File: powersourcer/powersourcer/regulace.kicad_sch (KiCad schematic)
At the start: 47 parts, among them Q1 2N2222, Q10 TIP35C, Q2 TIP122, Q3 TIP35C, Q4 TIP35C, Q5 TIP35C, Q6 TIP35C, Q7 TIP35C, Q8 TIP35C, Q9 TIP35C, U1 LM336Z-5.0, U2 TL081

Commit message: První návrh pcb.
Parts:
- C1, C2: footprint (none) -> Capacitor_SMD:C_1206_3216Metric_Pad1.33x1.80mm_HandSolder
- C3, C5: footprint (none) -> HAM_Lib:CP_Radial_D10.0mm_P5.00mm
- C4: footprint (none) -> HAM_Lib:CP_Radial_D8.0mm_P5.00mm
- H1, H2, H3, H4, H5, H6: footprint (none) -> HAM_Lib:PinHeader_1x01_P1.00mm_Vertical
- Q10, Q3, Q4, Q5, Q6, Q7, Q8, Q9: footprint HAM_Lib:TO-247-3_Vertical -> HAM_Lib:TO-247-3_Horizontal_TabUp
- R6: footprint (none) -> HAM_Lib:R_Radial_Power_L13.0mm_W9.0mm_P5.00mm
- RV1: footprint (none) -> HAM_Lib:Potentiometer_Bourns_3296W_Vertical
- U2: footprint (none) -> HAM_Lib:DIP-8_W7.62mm
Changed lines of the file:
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@@
 			)
 		)
-		(property "Footprint" ""
+		(property "Footprint" "HAM_Lib:PinHeader_1x01_P1.00mm_Vertical"
 			(at 20.32 24.13 0)
 			(hide yes)
@@
 			)
 		)
-		(property "Footprint" ""
+		(property "Footprint" "HAM_Lib:R_Radial_Power_L13.0mm_W9.0mm_P5.00mm"
 			(at 96.012 36.83 90)
 			(hide yes)
@@
 			)
 		)
-		(property "Footprint" ""
+		(property "Footprint" "HAM_Lib:DIP-8_W7.62mm"
 			(at 63.5 48.26 0)
 			(hide yes)
@@
 			)
 		)
-		(property "Footprint" ""
+		(property "Footprint" "HAM_Lib:CP_Radial_D10.0mm_P5.00mm"
 			(at 221.9452 35.56 0)
 			(hide yes)
@@
 			)
 		)
-		(property "Footprint" ""
+		(property "Footprint" "HAM_Lib:PinHeader_1x01_P1.00mm_Vertical"
 			(at 269.24 39.37 0)
 			(hide yes)
@@
 			)
 		)
-		(property "Footprint" ""
+		(property "Footprint" "HAM_Lib:PinHeader_1x01_P1.00mm_Vertical"
 			(at 113.03 41.91 0)
 			(hide yes)
@@
 			)
 		)
-		(property "Footprint" "HAM_Lib:TO-247-3_Vertical"
+		(property "Footprint" "HAM_Lib:TO-247-3_Horizontal_TabUp"
 			(at 237.49 60.325 0)
 			(hide yes)
@@
 			)
 		)
-		(property "Footprint" "HAM_Lib:TO-247-3_Vertical"
+		(property "Footprint" "HAM_Lib:TO-247-3_Horizontal_TabUp"
 			(at 219.71 60.325 0)
 			(hide yes)
@@
 			)
 		)
-		(property "Footprint" ""
+		(property "Footprint" "Capacitor_SMD:C_1206_3216Metric_Pad1.33x1.80mm_HandSolder"
 			(at 69.85 34.5948 0)
 			(hide yes)
@@
 			)
 		)
-		(property "Footprint" "HAM_Lib:TO-247-3_Vertical"
+		(property "Footprint" "HAM_Lib:TO-247-3_Horizontal_TabUp"
 			(at 201.93 60.325 0)
 			(hide yes)
@@
 			)
 		)
-		(property "Footprint" "HAM_Lib:TO-247-3_Vertical"
+		(property "Footprint" "HAM_Lib:TO-247-3_Horizontal_TabUp"
 			(at 166.37 60.325 0)
 			(hide yes)
@@
 			)
 		)
-		(property "Footprint" "HAM_Lib:TO-247-3_Vertical"
+		(property "Footprint" "HAM_Lib:TO-247-3_Horizontal_TabUp"
 			(at 255.27 60.325 0)
 			(hide yes)
@@
 			)
 		)
-		(property "Footprint" ""
+		(property "Footprint" "HAM_Lib:PinHeader_1x01_P1.00mm_Vertical"
 			(at 269.24 24.13 0)
 			(hide yes)
@@
 			)
 		)
-		(property "Footprint" ""
+		(property "Footprint" "HAM_Lib:CP_Radial_D10.0mm_P5.00mm"
 			(at 263.8552 35.56 0)
 			(hide yes)
@@
 			)
 		)
-		(property "Footprint" ""
+		(property "Footprint" "Capacitor_SMD:C_1206_3216Metric_Pad1.33x1.80mm_HandSolder"
 			(at 205.4352 35.56 0)
 			(hide yes)
@@
 			)
 		)
-		(property "Footprint" "HAM_Lib:TO-247-3_Vertical"
+		(property "Footprint" "HAM_Lib:TO-247-3_Horizontal_TabUp"
 			(at 148.59 60.325 0)
 			(hide yes)
@@
 			)
 		)
-		(property "Footprint" "HAM_Lib:TO-247-3_Vertical"
+		(property "Footprint" "HAM_Lib:TO-247-3_Horizontal_TabUp"
 			(at 184.15 60.325 0)
 			(hide yes)
@@
 			)
 		)
-		(property "Footprint" ""
+		(property "Footprint" "HAM_Lib:PinHeader_1x01_P1.00mm_Vertical"
 			(at 20.32 76.2 0)
 			(hide yes)
@@
 			)
 		)
-		(property "Footprint" ""
+		(property "Footprint" "HAM_Lib:Potentiometer_Bourns_3296W_Vertical"
 			(at 43.18 46.99 0)
 			(hide yes)
@@
 			)
 		)
-		(property "Footprint" "HAM_Lib:TO-247-3_Vertical"
+		(property "Footprint" "HAM_Lib:TO-247-3_Horizontal_TabUp"
 			(at 130.81 60.325 0)
 			(hide yes)
@@
 			)
 		)
-		(property "Footprint" ""
+		(property "Footprint" "HAM_Lib:PinHeader_1x01_P1.00mm_Vertical"
 			(at 113.03 29.21 0)
 			(hide yes)
@@
 			)
 		)
-		(property "Footprint" ""
+		(property "Footprint" "HAM_Lib:CP_Radial_D8.0mm_P5.00mm"
 			(at 240.9952 35.56 0)
 			(hide yes)

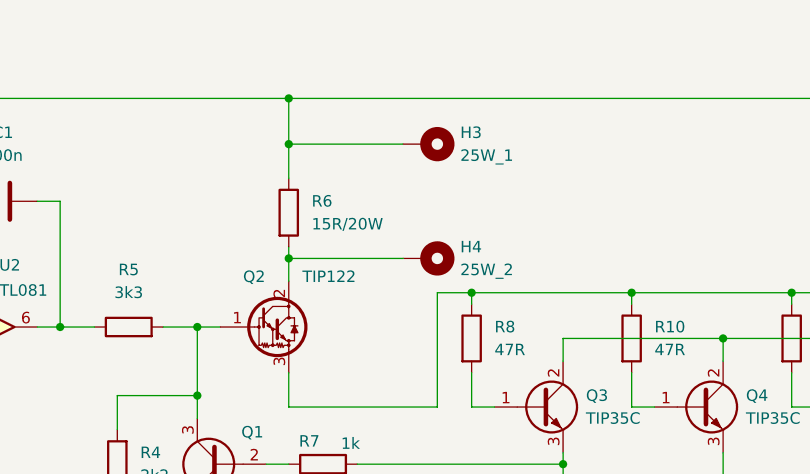
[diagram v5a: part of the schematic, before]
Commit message: Práce na pcb. Odstraněny plošky pro externí resistor.
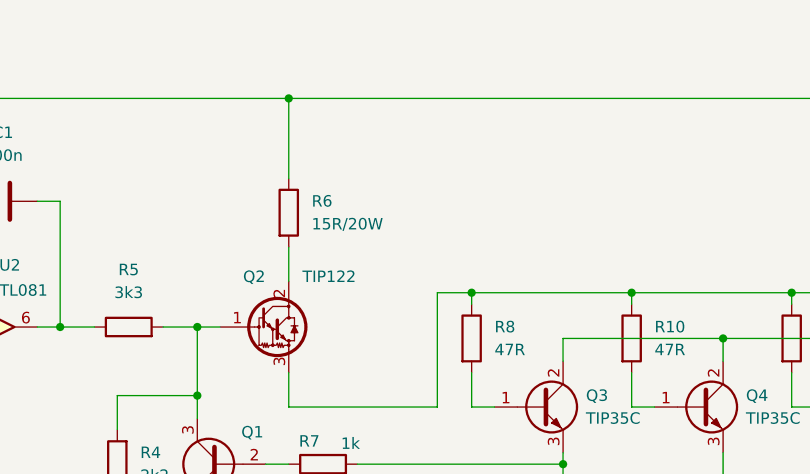
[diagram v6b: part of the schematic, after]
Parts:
- removed H3: 25W_1, HAM_Lib:PinHeader_1x01_P1.00mm_Vertical, symbol Mechanical:MountingHole_Pad_MP
- removed H4: 25W_2, HAM_Lib:PinHeader_1x01_P1.00mm_Vertical, symbol Mechanical:MountingHole_Pad_MP
- C3, C5: footprint HAM_Lib:CP_Radial_D10.0mm_P5.00mm -> HAM_Lib:CP_Radial_D22.0mm_P10.00mm_SnapIn
- C4: footprint HAM_Lib:CP_Radial_D8.0mm_P5.00mm -> HAM_Lib:CP_Radial_D10.0mm_P5.00mm
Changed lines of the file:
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@@
 	)
 	(junction
-		(at 97.79 41.91)
-		(diameter 0)
-		(color 0 0 0 0)
-	)
-	(junction
 		(at 49.53 46.99)
 		(diameter 0)
@@
 	)
 	(junction
-		(at 97.79 29.21)
-		(diameter 0)
-		(color 0 0 0 0)
-	)
-	(junction
 		(at 181.61 76.2)
 		(diameter 0)
@@
 	(wire
 		(pts
-			(xy 97.79 29.21) (xy 110.49 29.21)
-		)
-		(stroke
-			(width 0)
-			(type default)
-		)
-	)
-	(wire
-		(pts
 			(xy 72.39 35.56) (xy 72.39 49.53)
 		)
@@
 	(wire
 		(pts
-			(xy 97.79 29.21) (xy 97.79 33.02)
-		)
-		(stroke
-			(width 0)
-			(type default)
-		)
-	)
-	(wire
-		(pts
-			(xy 97.79 41.91) (xy 97.79 44.45)
+			(xy 97.79 24.13) (xy 97.79 33.02)
 		)
 		(stroke
@@
 	(wire
 		(pts
-			(xy 97.79 40.64) (xy 97.79 41.91)
+			(xy 97.79 40.64) (xy 97.79 44.45)
 		)
 		(stroke
@@
 	(wire
 		(pts
-			(xy 97.79 24.13) (xy 97.79 29.21)
-		)
-		(stroke
-			(width 0)
-			(type default)
-		)
-	)
-	(wire
-		(pts
 			(xy 97.79 54.61) (xy 97.79 58.42)
 		)
@@
 	(wire
 		(pts
-			(xy 97.79 41.91) (xy 110.49 41.91)
-		)
-		(stroke
-			(width 0)
-			(type default)
-		)
-	)
-	(wire
-		(pts
 			(xy 163.83 50.8) (xy 163.83 53.34)
 		)
@@
 			)
 		)
-		(property "Footprint" "HAM_Lib:CP_Radial_D10.0mm_P5.00mm"
+		(property "Footprint" "HAM_Lib:CP_Radial_D22.0mm_P10.00mm_SnapIn"
 			(at 221.9452 35.56 0)
 			(hide yes)
@@
 	)
 	(symbol
-		(lib_id "Mechanical:MountingHole_Pad_MP")
-		(at 113.03 41.91 270)
-		(unit 1)
-		(body_style 1)
-		(exclude_from_sim no)
-		(in_bom no)
-		(on_board yes)
-		(in_pos_files yes)
-		(dnp no)
-		(fields_autoplaced yes)
-		(property "Reference" "H4"
-			(at 116.84 40.6399 90)
-			(show_name no)
-			(do_not_autoplace no)
-			(effects
-				(font
-					(size 1.27 1.27)
-				)
-				(justify left)
-			)
-		)
-		(property "Value" "25W_2"
-			(at 116.84 43.1799 90)
-			(show_name no)
-			(do_not_autoplace no)
-			(effects
-				(font
-					(size 1.27 1.27)
-				)
-				(justify left)
-			)
-		)
-		(property "Footprint" "HAM_Lib:PinHeader_1x01_P1.00mm_Vertical"
-			(at 113.03 41.91 0)
-			(hide yes)
-			(show_name no)
-			(do_not_autoplace no)
-			(effects
-				(font
-					(size 1.27 1.27)
-				)
-			)
-		)
-		(property "Datasheet" ""
-			(at 113.03 41.91 0)
-			(hide yes)
-			(show_name no)
-			(do_not_autoplace no)
-			(effects
-				(font
-					(size 1.27 1.27)
-				)
-			)
-		)
-		(property "Description" "Mounting Hole with connection as pad named MP"
-			(at 113.03 41.91 0)
-			(hide yes)
-			(show_name no)
-			(do_not_autoplace no)
-			(effects
-				(font
-					(size 1.27 1.27)
-				)
-			)
-		)
-		(pin "MP"
-		)
-		(instances
-			(project "powersourcer"
-				(path "/3b543968-b752-41ec-9e14-3a471f109ffc/57492013-ce66-4b1a-aeb4-b7d85251d918"
-					(reference "H4")
-					(unit 1)
-				)
-			)
-		)
-	)
-	(symbol
 		(lib_id "Transistor_BJT:TIP3055G")
 		(at 232.41 58.42 0)
@@
 			)
 		)
-		(property "Footprint" "HAM_Lib:CP_Radial_D10.0mm_P5.00mm"
+		(property "Footprint" "HAM_Lib:CP_Radial_D22.0mm_P10.00mm_SnapIn"
 			(at 263.8552 35.56 0)
 			(hide yes)
@@
 	)
 	(symbol
-		(lib_id "Mechanical:MountingHole_Pad_MP")
-		(at 113.03 29.21 270)
-		(unit 1)
-		(body_style 1)
-		(exclude_from_sim no)
-		(in_bom no)
-		(on_board yes)
-		(in_pos_files yes)
-		(dnp no)
-		(fields_autoplaced yes)
-		(property "Reference" "H3"
-			(at 116.84 27.9399 90)
-			(show_name no)
-			(do_not_autoplace no)
-			(effects
-				(font
-					(size 1.27 1.27)
-				)
-				(justify left)
-			)
-		)
-		(property "Value" "25W_1"
-			(at 116.84 30.4799 90)
-			(show_name no)
-			(do_not_autoplace no)
-			(effects
-				(font
-					(size 1.27 1.27)
-				)
-				(justify left)
-			)
-		)
-		(property "Footprint" "HAM_Lib:PinHeader_1x01_P1.00mm_Vertical"
-			(at 113.03 29.21 0)
-			(hide yes)
-			(show_name no)
-			(do_not_autoplace no)
-			(effects
-				(font
-					(size 1.27 1.27)
-				)
-			)
-		)
-		(property "Datasheet" ""
-			(at 113.03 29.21 0)
-			(hide yes)
-			(show_name no)
-			(do_not_autoplace no)
-			(effects
-				(font
-					(size 1.27 1.27)
-				)
-			)
-		)
-		(property "Description" "Mounting Hole with connection as pad named MP"
-			(at 113.03 29.21 0)
-			(hide yes)
-			(show_name no)
-			(do_not_autoplace no)
-			(effects
-				(font
-					(size 1.27 1.27)
-				)
-			)
-		)
-		(pin "MP"
-		)
-		(instances
-			(project "powersourcer"
-				(path "/3b543968-b752-41ec-9e14-3a471f109ffc/57492013-ce66-4b1a-aeb4-b7d85251d918"
-					(reference "H3")
-					(unit 1)
-				)
-			)
-		)
-	)
-	(symbol
 		(lib_id "Device:R")
 		(at 242.57 50.8 0)
@@
 			)
 		)
-		(property "Footprint" "HAM_Lib:CP_Radial_D8.0mm_P5.00mm"
+		(property "Footprint" "HAM_Lib:CP_Radial_D10.0mm_P5.00mm"
 			(at 240.9952 35.56 0)
 			(hide yes)
